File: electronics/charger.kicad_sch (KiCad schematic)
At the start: 14 parts, among them J5 Conn_01x02_MountingPin, Q1 DMG2305UX, SW3 SW_SPDT, U3 AP2112K-3.3, U33 MCP73831-2-MC

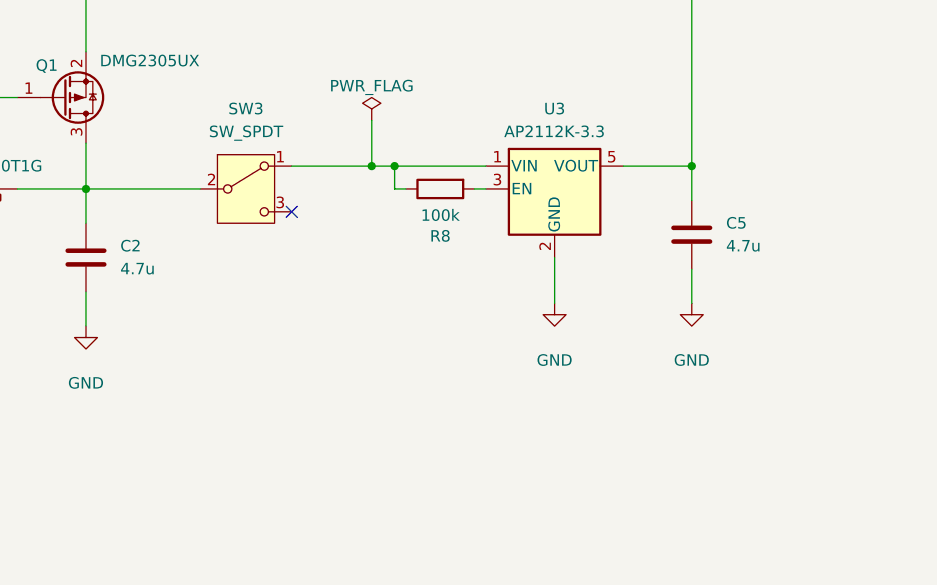
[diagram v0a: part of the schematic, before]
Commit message: electronics: start with A7670 module
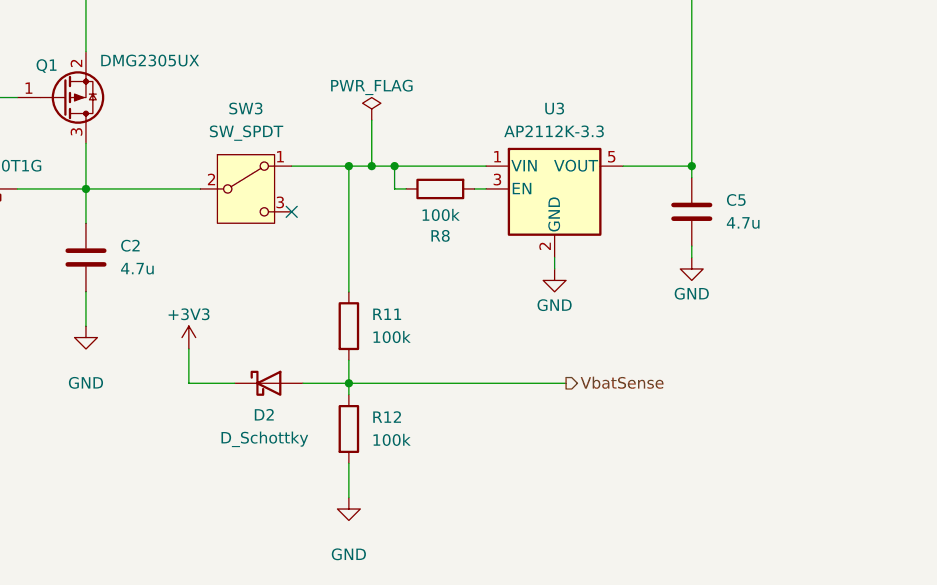
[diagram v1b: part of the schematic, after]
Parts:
- added D2: D_Schottky, symbol Device:D_Schottky
- added R11, R12: 100k, Resistor_SMD:R_0603_1608Metric, symbol Device:R
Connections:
- net +3V3: now also D2.1 (K)
- net GND: now also R12.2
- net at R8.1, SW3.1 (A), U3.1 (VIN): now also R11.1
- new net VbatSense: D2.2 (A), R11.2, R12.1
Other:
- moved on the sheet: C5

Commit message: schematics
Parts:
- removed U3: AP2112K-3.3, Package_TO_SOT_SMD:SOT-23-5, symbol Regulator_Linear:AP2112K-3.3
- added C35: 1u, Capacitor_SMD:C_0603_1608Metric, symbol Device:C
- added U6: TPS7A0518PDBV, Package_TO_SOT_SMD:SOT-23-5, symbol Regulator_Linear:TPS7A0518PDBV
- C5: value 4.7u -> 1u
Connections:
- net GND: now also C35.2, U6.2 (GND)
- net VBAT: now also R11.1, R8.1, SW3.1 (A), C35.1, U6.1 (IN); no longer C6.1, J5.1 (Pin_1), Q1.2 (S), U33.3 (V_{BAT}), U33.4 (V_{BAT})
- net at R8.2: now also U6.3 (EN)
- net +3V3 renamed +1V8
- net +1V8: now also U6.5 (OUT)
- new net Vpack: C6.1, J5.1 (Pin_1), Q1.2 (S), U33.3 (V_{BAT}), U33.4 (V_{BAT})
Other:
- moved on the sheet: C5, R11, R8

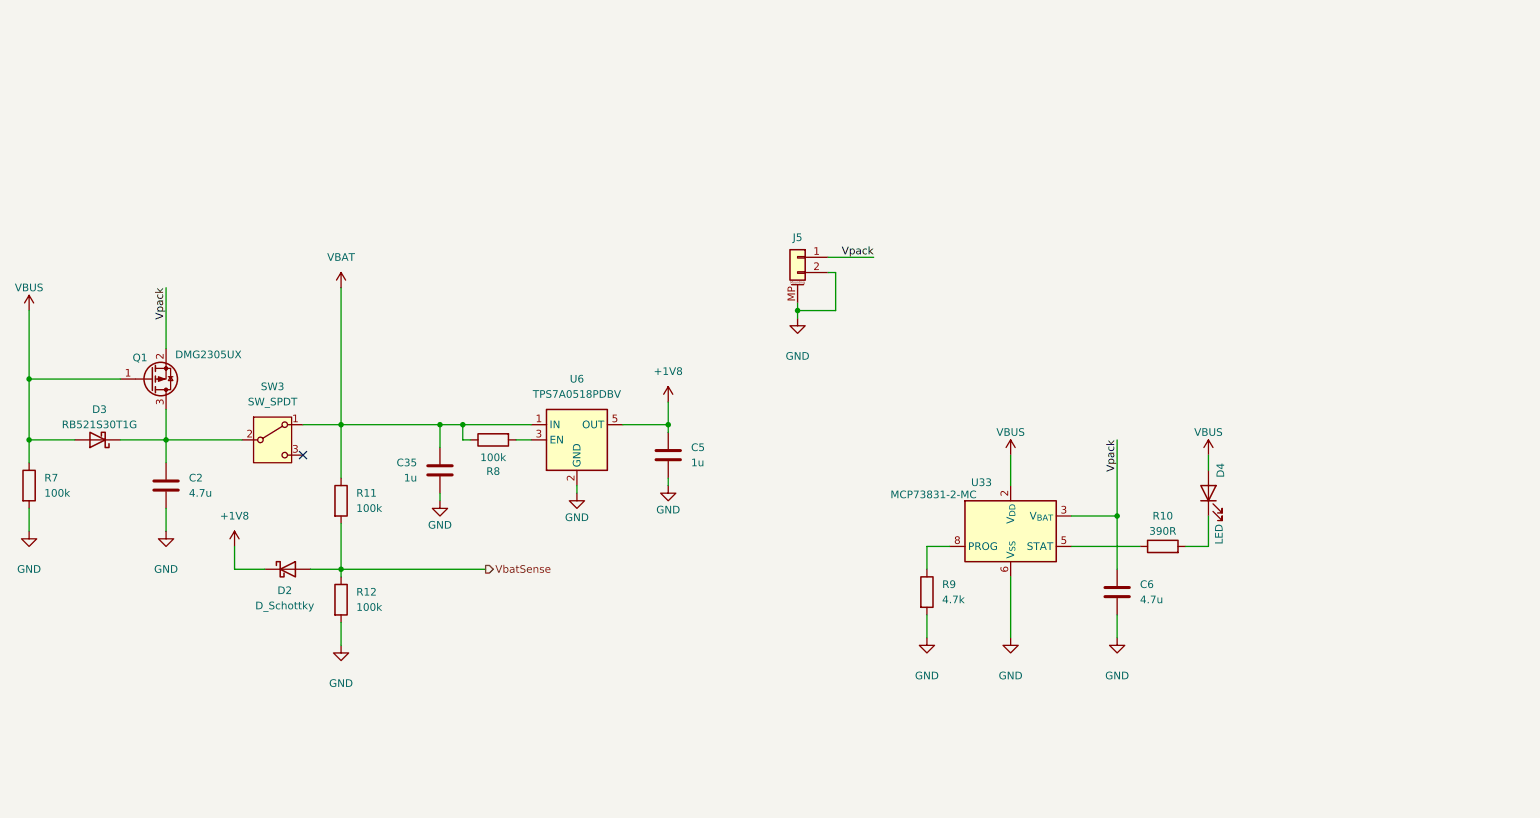
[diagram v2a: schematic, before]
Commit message: electronics: replace charger
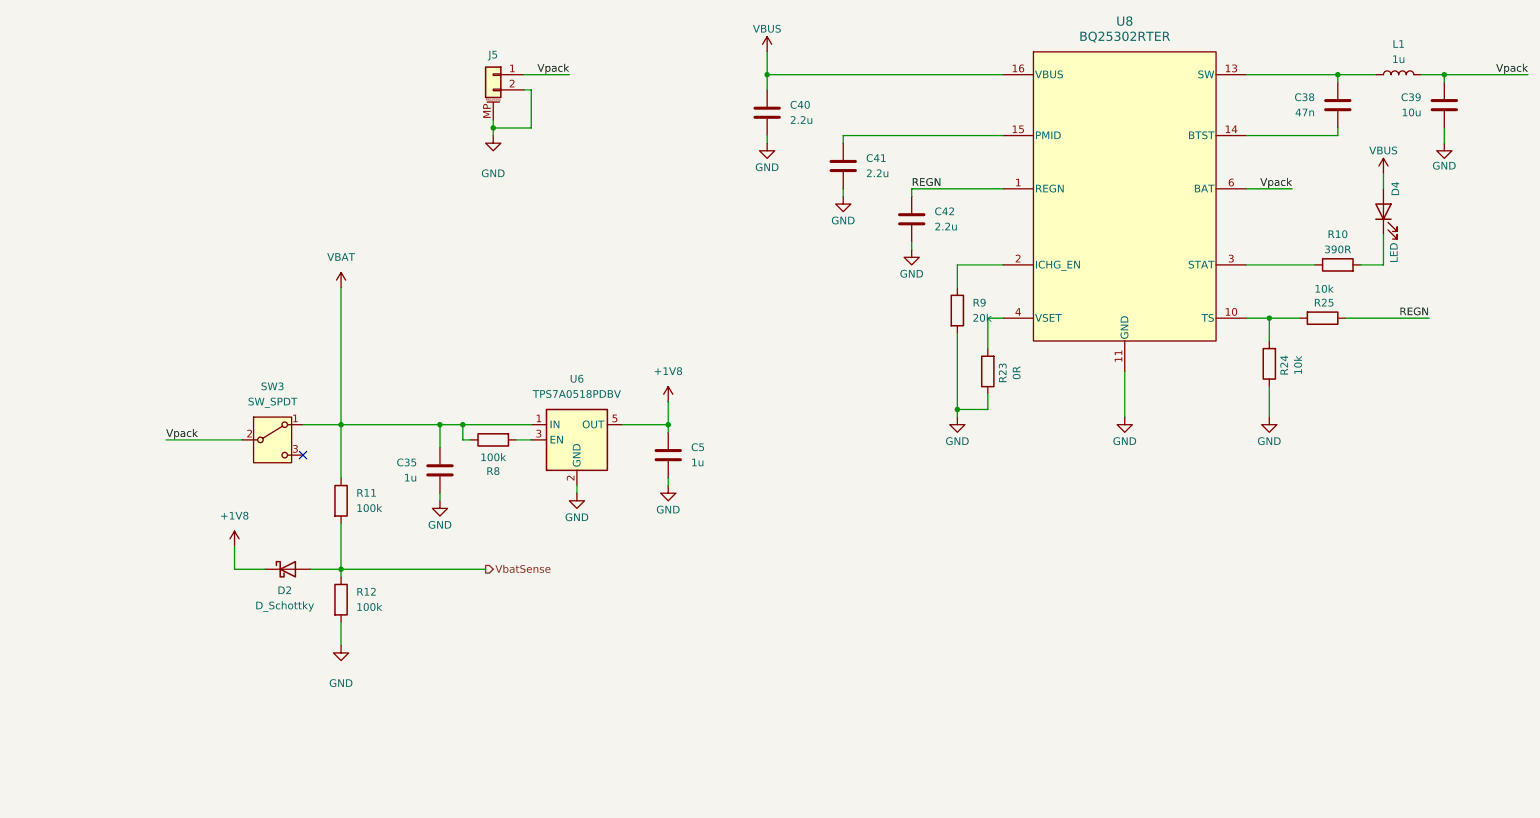
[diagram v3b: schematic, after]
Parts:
- removed C2, C6: 4.7u, Capacitor_SMD:C_0603_1608Metric, symbol Device:C
- removed D3: RB521S30T1G, Diode_SMD:D_SOD-523, symbol Device:D_Schottky
- removed Q1: DMG2305UX, Package_TO_SOT_SMD:SOT-23, symbol Transistor_FET:Q_PMOS_GSD
- removed R7: 100k, Resistor_SMD:R_0603_1608Metric, symbol Device:R
- removed U33: MCP73831-2-MC, MyScale:MCP_73831-2-MC, symbol MyScale:MCP73831-2-MC
- added C38: 47n, Capacitor_SMD:C_0603_1608Metric, symbol Device:C
- added C39: 10u, Capacitor_SMD:C_0805_2012Metric, symbol Device:C
- added C40, C41, C42: 2.2u, Capacitor_SMD:C_0603_1608Metric, symbol Device:C
- added L1: 1u, symbol Device:L
- added R23: 0R, Resistor_SMD:R_0603_1608Metric, symbol Device:R
- added R24, R25: 10k, Resistor_SMD:R_0603_1608Metric, symbol Device:R
- added U8: BQ25302RTER, MyScale:TI_RTE0016C, symbol MyScale:BQ25302RTER
- R9: value 4.7k -> 20k
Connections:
- net GND: now also C39.2, C40.2, C41.2, C42.2, R23.1, R24.1, U8.11 (GND), U8.12 (GND), U8.17 (PAD)
- net VBUS: now also C40.1, U8.16 (VBUS)
- net Vpack: now also SW3.2 (B), C39.1, L1.2, U8.6 (BAT)
- net at R10.1: now also U8.3 (STAT)
- net at R9.1: now also U8.2 (ICHG_EN)
- new net: R24.2, R25.2, U8.10 (TS)
- new net: C38.1, L1.1, U8.13 (SW)
- new net: C38.2, U8.14 (BTST)
- new net: R23.2, U8.4 (VSET)
- new net: C41.1, U8.15 (PMID)
- new net: U8.5 (NC), U8.7 (NC), U8.8 (NC), U8.9 (NC)
- new net REGN: C42.1, R25.1, U8.1 (REGN)
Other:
- moved on the sheet: D4, J5, R10, R9

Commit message: electronics: initial placement
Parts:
- C41: value 2.2u -> 10u; footprint Capacitor_SMD:C_0603_1608Metric -> Capacitor_SMD:C_0805_2012Metric
- D2: footprint (none) -> Diode_SMD:D_SOD-523; MPN (none) -> BAT30KFILM
- L1: footprint (none) -> MyScale:MG_MAPM0420F
- R11: value 100k -> 20k
- R12: value 100k -> 10k
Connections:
- net REGN: now also U8.2 (REGN); no longer U8.1 (REGN)
- net VBUS: now also U8.1 (VBUS); no longer U8.16 (VBUS)
- net Vpack: now also U8.10 (BAT); no longer U8.6 (BAT)
- net at R24.2, R25.2: now also U8.7 (TS); no longer U8.10 (TS)
- net at C38.1, L1.1, U8.13 (SW): now also U8.14 (SW)
- net at C38.2: now also U8.15 (BTST); no longer U8.14 (BTST)
- net at R23.2: now also U8.9 (VSET); no longer U8.4 (VSET)
- net at R9.1: now also U8.4 (ICHG_EN); no longer U8.2 (ICHG_EN)
- net at C41.1: now also U8.16 (PMID); no longer U8.15 (PMID)
- net at U8.5 (POL), U8.8 (NC): no longer U8.7 (NC), U8.9 (NC)
- no-connect marks 1 -> 2
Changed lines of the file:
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@@
 	)
 	(no_connect
+		(at 208.28 36.83)
+	)
+	(no_connect
 		(at 91.44 97.79)
 	)
@@
 			)
 		)
-		(property "Footprint" ""
+		(property "Footprint" "Diode_SMD:D_SOD-523"
 			(at 88.9 116.84 0)
 			(hide yes)
@@
 			)
 		)
+		(property "MPN" "BAT30KFILM"
+			(at 88.9 116.84 0)
+			(hide yes)
+			(show_name no)
+			(do_not_autoplace no)
+			(effects
+				(font
+					(size 1.27 1.27)
+				)
+			)
+		)
 		(pin "1"
 		)
@@
 			)
 		)
-		(property "Footprint" ""
+		(property "Footprint" "MyScale:MG_MAPM0420F"
 			(at 274.32 34.29 0)
 			(hide yes)
@@
 			)
 		)
-		(property "Value" "100k"
+		(property "Value" "20k"
 			(at 100.33 106.6799 0)
 			(show_name no)
@@
 			)
 		)
-		(property "Value" "2.2u"
+		(property "Value" "10u"
 			(at 185.42 50.7999 0)
 			(show_name no)
@@
 			)
 		)
-		(property "Footprint" "Capacitor_SMD:C_0603_1608Metric"
+		(property "Footprint" "Capacitor_SMD:C_0805_2012Metric"
 			(at 182.5752 53.34 0)
 			(hide yes)
@@
 			)
 		)
-		(property "Value" "100k"
+		(property "Value" "10k"
 			(at 100.33 123.1899 0)
 			(show_name no)

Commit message: electronics: start routing
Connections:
- net VBAT: now also SW3.3 (C); no longer SW3.1 (A)
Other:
- moved on the sheet: SW3
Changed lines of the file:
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@@
 	)
 	(no_connect
-		(at 91.44 97.79)
+		(at 91.44 87.63)
 	)
 	(wire
@@
 	(wire
 		(pts
-			(xy 68.58 95.25) (xy 81.28 95.25)
+			(xy 68.58 90.17) (xy 81.28 90.17)
 		)
 		(stroke
@@
 	)
 	(label "Vpack"
-		(at 68.58 95.25 0)
+		(at 68.58 90.17 0)
 		(effects
 			(font
@@
 	(symbol
 		(lib_id "Switch:SW_SPDT")
-		(at 86.36 95.25 0)
+		(at 86.36 90.17 0)
 		(unit 1)
 		(body_style 1)
@@
 		(fields_autoplaced yes)
 		(property "Reference" "SW3"
-			(at 86.36 86.36 0)
+			(at 86.36 81.28 0)
 			(show_name no)
 			(do_not_autoplace no)
@@
 		)
 		(property "Value" "SW_SPDT"
-			(at 86.36 88.9 0)
+			(at 86.36 83.82 0)
 			(show_name no)
 			(do_not_autoplace no)
@@
 		)
 		(property "Footprint" "MyScale:CAK_AYZ0102AURLC"
-			(at 86.36 95.25 0)
+			(at 86.36 90.17 0)
 			(hide yes)
 			(show_name no)
@@
 		)
 		(property "Datasheet" ""
-			(at 86.36 102.87 0)
+			(at 86.36 97.79 0)
 			(hide yes)
 			(show_name no)
@@
 		)
 		(property "Description" "Switch, single pole double throw"
-			(at 86.36 95.25 0)
+			(at 86.36 90.17 0)
 			(hide yes)
 			(show_name no)
@@
 		)
 		(property "MPN" "AYZ0102AURLC"
-			(at 86.36 95.25 0)
-			(hide yes)
-			(show_name no)
+			(at 86.36 90.17 0)
+			(hide yes)
+			(show_name no)

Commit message: electronics: more routing
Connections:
- net at U8.5 (POL): no longer U8.8 (NC)

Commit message: electronics: final touches
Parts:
- added Q2: Q_NMOS_GSD, Package_TO_SOT_SMD:SOT-23-3, symbol Transistor_FET:Q_NMOS_GSD
- added R30: 10k, Resistor_SMD:R_0603_1608Metric, symbol Device:R
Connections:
- net GND: now also Q2.2 (S), R30.2; no longer R12.2
- new net: Q2.3 (D), R12.2
- new net BatSenseEnable: Q2.1 (G), R30.1

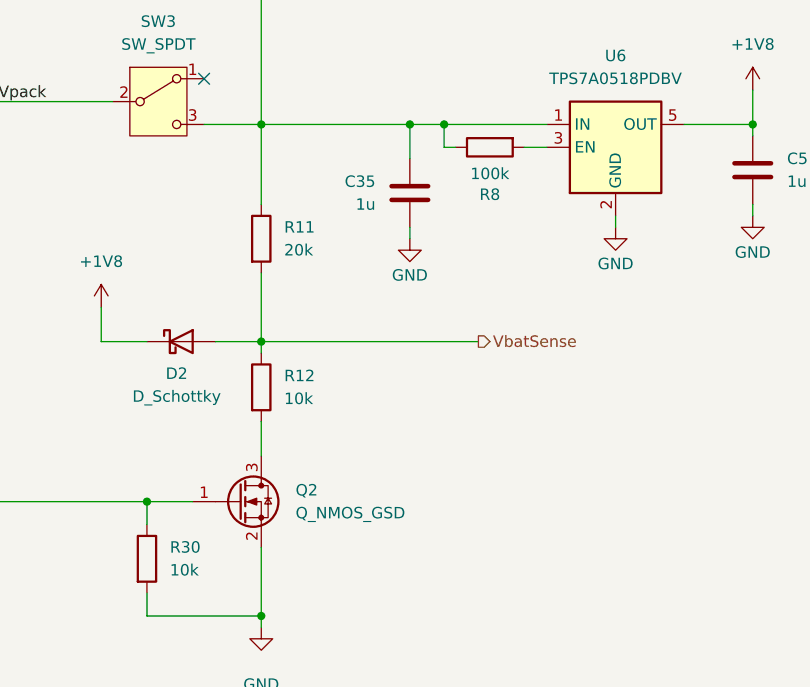
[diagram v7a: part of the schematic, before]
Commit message: electronics: add MPNs
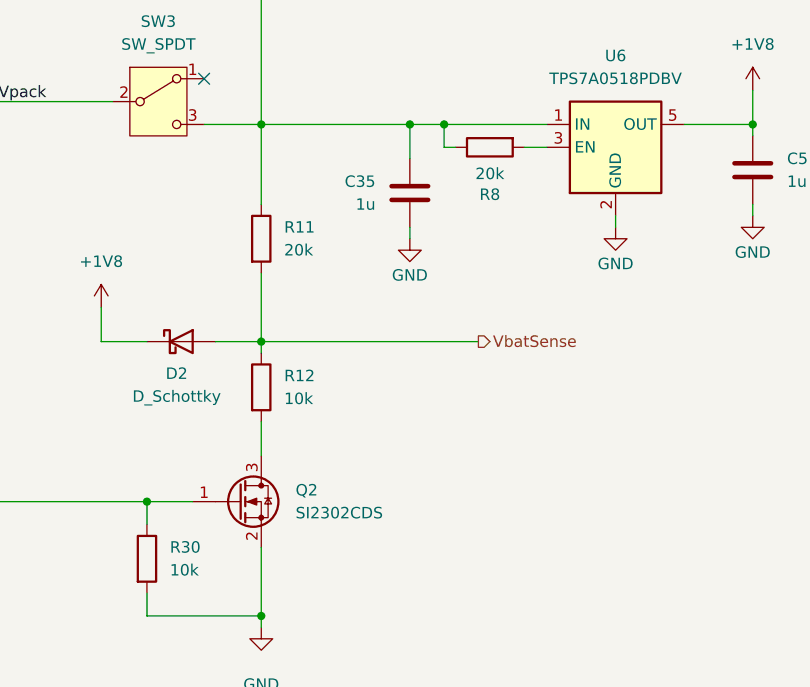
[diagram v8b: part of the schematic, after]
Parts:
- Q2: value Q_NMOS_GSD -> SI2302CDS; MPN (none) -> SI2302CDS-T1-GE3
- R8: value 100k -> 20k
- U6: MPN (none) -> TPS7A0518PDBV
- U8: MPN (none) -> BQ25302RTER
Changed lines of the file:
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@@
 			)
 		)
-		(property "Value" "100k"
+		(property "Value" "20k"
 			(at 123.19 98.1964 90)
 			(show_name no)
@@
 			)
 		)
+		(property "MPN" "TPS7A0518PDBV"
+			(at 137.16 95.25 0)
+			(hide yes)
+			(show_name no)
+			(do_not_autoplace no)
+			(effects
+				(font
+					(size 1.27 1.27)
+				)
+			)
+		)
 		(pin "2"
 		)
@@
 			)
 		)
-		(property "Value" "Q_NMOS_GSD"
+		(property "Value" "SI2302CDS"
 			(at 101.6 135.8899 0)
 			(show_name no)
@@
 		)
 		(property "Description" "N-MOSFET transistor, gate/source/drain"
+			(at 95.25 134.62 0)
+			(hide yes)
+			(show_name no)
+			(do_not_autoplace no)
+			(effects
+				(font
+					(size 1.27 1.27)
+				)
+			)
+		)
+		(property "MPN" "SI2302CDS-T1-GE3"
 			(at 95.25 134.62 0)
 			(hide yes)
@@
 			(at 228.6 55.88 0)
 			(hide yes)
+			(show_name no)
+			(do_not_autoplace no)
+			(effects
+				(font
+					(size 1.27 1.27)
+				)
+			)
+		)
+		(property "MPN" "BQ25302RTER"
+			(at 228.6 55.88 0)
+			(hide yes)
